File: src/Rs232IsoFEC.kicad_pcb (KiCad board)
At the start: 2 copper layers, 24 x 27.9 mm, 24 parts, among them J1 B3B-XH-A, P1 105444-0001, Q1 DMP3099L-13, U1 FT232RL, U2 ADM3251E

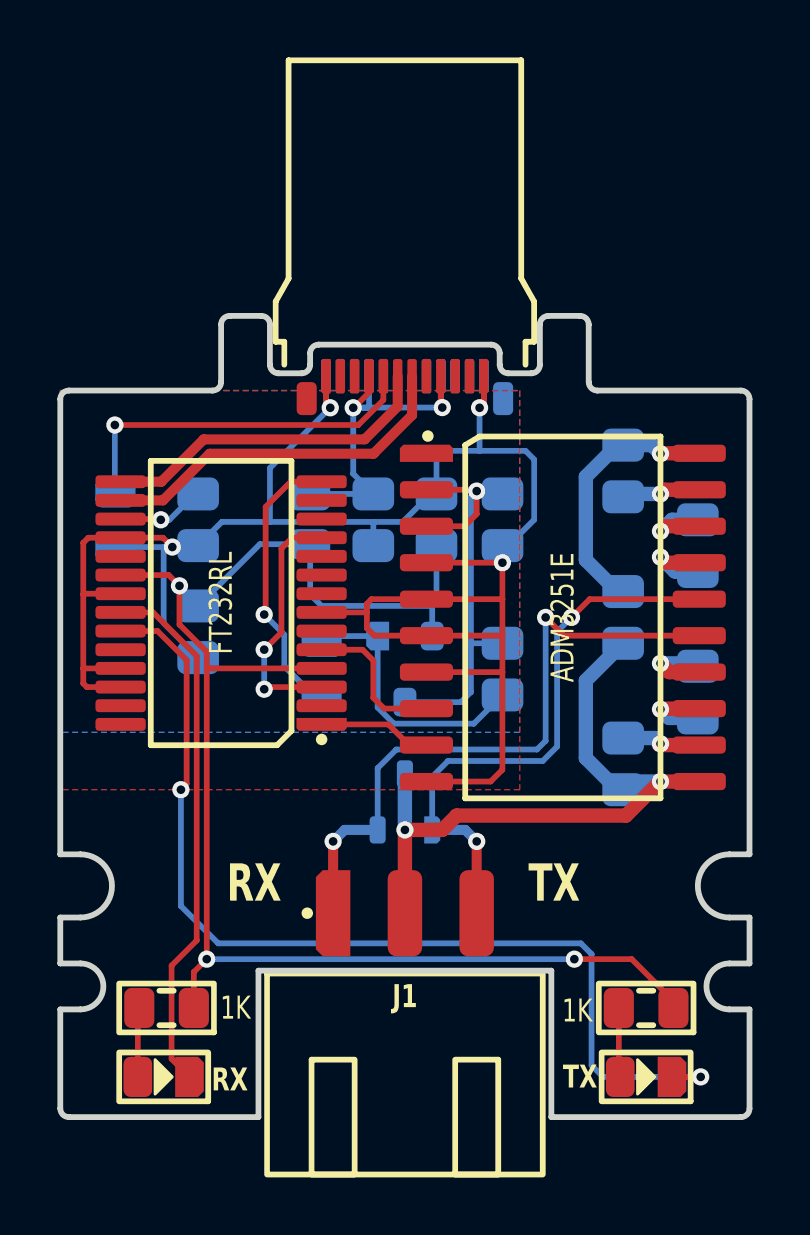
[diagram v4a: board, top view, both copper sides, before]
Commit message: Changed protection diode
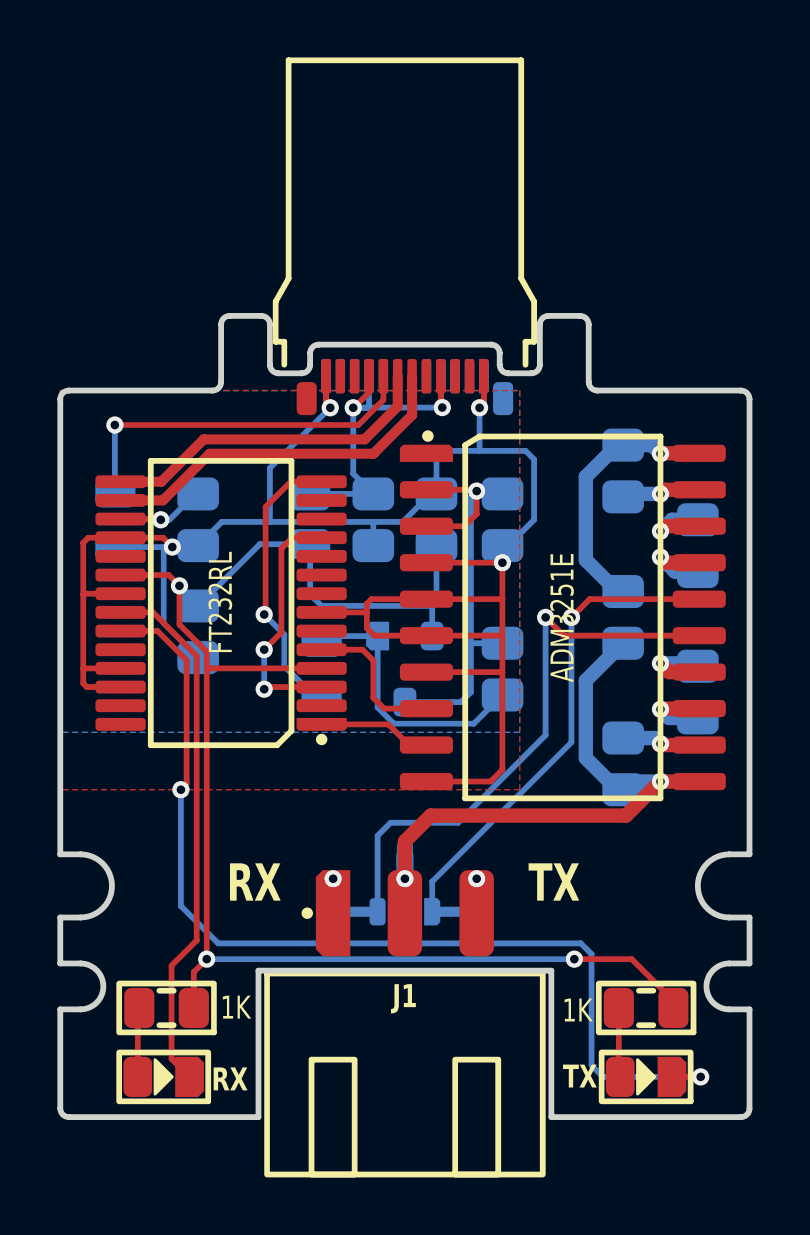
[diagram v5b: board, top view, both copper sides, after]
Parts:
- D1: value SM12T1G -> PESD12VL2BT
- moved D1 2.85 mm to (32.0, 39.8)
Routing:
- net ISO_GND: track 22.9 -> 20.3 mm
- net ISO_TXD: track 20.3 -> 19.7 mm
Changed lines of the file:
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@@
   )
   (footprint "Medo64:D TVS SM05T1G (SOT23-3)" (layer "B.Cu")
-    (at 32 36.925 180)
+    (at 32 39.775 180)
     (descr "SM05T1G [SM05T1GOSCT-ND]")
     (attr smd)
@@
         (effects (font (size 0.8 0.6) (thickness 0.15)) (justify mirror))
     )
-    (fp_text value "SM12T1G" (at 0 -2.2) (layer "B.SilkS") hide
+    (fp_text value "PESD12VL2BT" (at 0 -2.2) (layer "B.SilkS") hide
         (effects (font (size 0.8 0.6) (thickness 0.15)) (justify mirror))
     )
@@
   (segment (start 23.875 42.625) (end 23.875 45.875) (width 0.2) (layer "F.Cu") (net 13))
   (segment (start 22.1 30.325) (end 23.230026 30.325) (width 0.2) (layer "F.Cu") (net 13))
+  (segment (start 32.9 37.4) (end 39.7 37.4) (width 0.5) (layer "F.Cu") (net 14))
+  (segment (start 40.9 36.215) (end 42.25 36.215) (width 0.5) (layer "F.Cu") (net 14))
   (segment (start 40.885 36.215) (end 40.9 36.215) (width 0.5) (layer "F.Cu") (net 14))
-  (segment (start 33.8 37.4) (end 39.7 37.4) (width 0.5) (layer "F.Cu") (net 14))
-  (segment (start 32 37.9) (end 33.3 37.9) (width 0.5) (layer "F.Cu") (net 14))
-  (segment (start 33.3 37.9) (end 33.8 37.4) (width 0.5) (layer "F.Cu") (net 14))
+  (segment (start 32 38.3) (end 32.9 37.4) (width 0.5) (layer "F.Cu") (net 14))
   (segment (start 39.7 37.4) (end 40.885 36.215) (width 0.5) (layer "F.Cu") (net 14))
-  (segment (start 40.9 36.215) (end 42.25 36.215) (width 0.5) (layer "F.Cu") (net 14))
-  (segment (start 32 40.8) (end 32 37.9) (width 0.5) (layer "F.Cu") (net 14))
-  (via (at 32 37.9) (size 0.6) (drill 0.3) (layers "F.Cu" "B.Cu") (net 14))
+  (segment (start 32 39.6) (end 32 38.3) (width 0.5) (layer "F.Cu") (net 14))
+  (via (at 32 39.6) (size 0.6) (drill 0.3) (layers "F.Cu" "B.Cu") (net 14))
   (via (at 40.9 36.215) (size 0.6) (drill 0.3) (layers "F.Cu" "B.Cu") (net 14))
   (segment (start 39.4 36.5) (end 38.3 35.4) (width 0.5) (layer "B.Cu") (net 14))
-  (segment (start 32 37.9) (end 32 35.95) (width 0.5) (layer "B.Cu") (net 14))
+  (segment (start 32 38.8) (end 32 39.6) (width 0.6) (layer "B.Cu") (net 14))
   (segment (start 38.3 35.4) (end 38.3 32.7) (width 0.5) (layer "B.Cu") (net 14))
   (segment (start 40.9 36.215) (end 39.885 36.215) (width 0.5) (layer "B.Cu") (net 14))
   (segment (start 38.3 32.7) (end 39.6 31.4) (width 0.5) (layer "B.Cu") (net 14))
-  (segment (start 29.5 40.8) (end 29.5 38.3) (width 0.35) (layer "F.Cu") (net 15))
   (segment (start 42.25 31.135) (end 37.535 31.135) (width 0.2) (layer "F.Cu") (net 15))
   (segment (start 37.535 31.135) (end 36.9 30.5) (width 0.2) (layer "F.Cu") (net 15))
-  (via (at 29.5 38.3) (size 0.6) (drill 0.3) (layers "F.Cu" "B.Cu") (net 15))
+  (via (at 29.5 39.6) (size 0.6) (drill 0.3) (layers "F.Cu" "B.Cu") (net 15))
   (via (at 36.9 30.5) (size 0.6) (drill 0.3) (layers "F.Cu" "B.Cu") (net 15))
-  (segment (start 29.9 37.9) (end 31.05 37.9) (width 0.35) (layer "B.Cu") (net 15))
-  (segment (start 36.9 34.8) (end 36.9 30.5) (width 0.2) (layer "B.Cu") (net 15))
-  (segment (start 31.05 35.75) (end 31.7 35.1) (width 0.2) (layer "B.Cu") (net 15))
-  (segment (start 31.7 35.1) (end 36.6 35.1) (width 0.2) (layer "B.Cu") (net 15))
-  (segment (start 29.5 38.3) (end 29.9 37.9) (width 0.35) (layer "B.Cu") (net 15))
-  (segment (start 36.6 35.1) (end 36.9 34.8) (width 0.2) (layer "B.Cu") (net 15))
-  (segment (start 31.05 37.9) (end 31.05 35.75) (width 0.2) (layer "B.Cu") (net 15))
+  (segment (start 31.05 38.1) (end 31.05 40.750002) (width 0.2) (layer "B.Cu") (net 15))
+  (segment (start 29.5 40.750002) (end 31.05 40.750002) (width 0.35) (layer "B.Cu") (net 15))
+  (segment (start 33.85 37.65) (end 31.5 37.65) (width 0.2) (layer "B.Cu") (net 15))
+  (segment (start 31.5 37.65) (end 31.05 38.1) (width 0.2) (layer "B.Cu") (net 15))
+  (segment (start 36.9 30.5) (end 36.9 34.6) (width 0.2) (layer "B.Cu") (net 15))
+  (segment (start 36.9 34.6) (end 33.85 37.65) (width 0.2) (layer "B.Cu") (net 15))
+  (segment (start 29.5 39.6) (end 29.5 40.750002) (width 0.35) (layer "B.Cu") (net 15))
   (segment (start 42.25 29.865) (end 38.435 29.865) (width 0.2) (layer "F.Cu") (net 16))
   (segment (start 38.435 29.865) (end 37.8 30.5) (width 0.2) (layer "F.Cu") (net 16))
-  (segment (start 34.5 40.8) (end 34.5 38.3) (width 0.35) (layer "F.Cu") (net 16))
-  (via (at 34.5 38.3) (size 0.6) (drill 0.3) (layers "F.Cu" "B.Cu") (net 16))
+  (via (at 34.5 39.6) (size 0.6) (drill 0.3) (layers "F.Cu" "B.Cu") (net 16))
   (via (at 37.8 30.5) (size 0.6) (drill 0.3) (layers "F.Cu" "B.Cu") (net 16))
-  (segment (start 32.95 37.9) (end 32.95 36.05) (width 0.2) (layer "B.Cu") (net 16))
-  (segment (start 33.5 35.5) (end 36.8 35.5) (width 0.2) (layer "B.Cu") (net 16))
-  (segment (start 37.3 35) (end 37.3 31) (width 0.2) (layer "B.Cu") (net 16))
-  (segment (start 34.1 37.9) (end 32.95 37.9) (width 0.35) (layer "B.Cu") (net 16))
-  (segment (start 37.3 31) (end 37.8 30.5) (width 0.2) (layer "B.Cu") (net 16))
-  (segment (start 34.5 38.3) (end 34.1 37.9) (width 0.35) (layer "B.Cu") (net 16))
-  (segment (start 32.95 36.05) (end 33.5 35.5) (width 0.2) (layer "B.Cu") (net 16))
-  (segment (start 36.8 35.5) (end 37.3 35) (width 0.2) (layer "B.Cu") (net 16))
+  (segment (start 34.5 39.6) (end 34.5 40.750002) (width 0.35) (layer "B.Cu") (net 16))
+  (segment (start 34.5 40.750002) (end 32.95 40.750002) (width 0.35) (layer "B.Cu") (net 16))
+  (segment (start 32.95 39.7) (end 32.95 40.750002) (width 0.2) (layer "B.Cu") (net 16))
+  (segment (start 37.8 34.85) (end 32.95 39.7) (width 0.2) (layer "B.Cu") (net 16))
+  (segment (start 37.8 30.5) (end 37.8 34.85) (width 0.2) (layer "B.Cu") (net 16))
   (segment (start 41.045 26.055) (end 40.9 26.2) (width 0.5) (layer "F.Cu") (net 17))
   (segment (start 42.25 26.055) (end 41.045 26.055) (width 0.5) (layer "F.Cu") (net 17))

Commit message: Minor refactoring
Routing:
- net ISO_TXD: track 19.7 -> 18.5 mm
- net ISO_RXD: track 22.4 -> 21.2 mm
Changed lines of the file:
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@@
     (descr "SM05T1G [SM05T1GOSCT-ND]")
     (attr smd)
-    (fp_text reference "D1" (at -1.2 1.425) (layer "B.SilkS")
+    (fp_text reference "D1" (at 0 -0.975) (layer "B.SilkS")
         (effects (font (size 0.8 0.6) (thickness 0.15)) (justify mirror))
     )
@@
   (gr_circle locked (center 20.7 39.85) (end 23.15 39.85)
     (stroke (width 0.01) (type solid)) (fill none) (layer "Margin"))
-  (gr_text "Rs232IsoFEC A" (at 32 41.8) (layer "B.SilkS")
+  (gr_text "Rs232IsoFEC A" (at 32 37.5) (layer "B.SilkS")
     (effects (font (size 0.8 0.6) (thickness 0.15) bold) (justify mirror))
   )
-  (gr_text "RX" (at 27.7 39) (layer "F.SilkS" knockout)
+  (gr_text "RX" (at 27.95 39) (layer "F.SilkS" knockout)
     (effects (font (size 1.3 0.9) (thickness 0.15) bold) (justify right top))
   )
-  (gr_text "TX" (at 36.3 39) (layer "F.SilkS" knockout)
+  (gr_text "TX" (at 36.05 39) (layer "F.SilkS" knockout)
     (effects (font (size 1.3 0.9) (thickness 0.15) bold) (justify left top))
   )
@@
   (segment (start 42.25 31.135) (end 37.535 31.135) (width 0.2) (layer "F.Cu") (net 15))
   (segment (start 37.535 31.135) (end 36.9 30.5) (width 0.2) (layer "F.Cu") (net 15))
-  (via (at 29.5 39.6) (size 0.6) (drill 0.3) (layers "F.Cu" "B.Cu") (net 15))
+  (via (at 29.5 40.75) (size 0.6) (drill 0.3) (layers "F.Cu" "B.Cu") (net 15))
   (via (at 36.9 30.5) (size 0.6) (drill 0.3) (layers "F.Cu" "B.Cu") (net 15))
   (segment (start 31.05 38.1) (end 31.05 40.750002) (width 0.2) (layer "B.Cu") (net 15))
-  (segment (start 29.5 40.750002) (end 31.05 40.750002) (width 0.35) (layer "B.Cu") (net 15))
+  (segment (start 29.5 40.75) (end 29.500002 40.750002) (width 0.35) (layer "B.Cu") (net 15))
   (segment (start 33.85 37.65) (end 31.5 37.65) (width 0.2) (layer "B.Cu") (net 15))
   (segment (start 31.5 37.65) (end 31.05 38.1) (width 0.2) (layer "B.Cu") (net 15))
+  (segment (start 29.500002 40.750002) (end 31.05 40.750002) (width 0.35) (layer "B.Cu") (net 15))
   (segment (start 36.9 30.5) (end 36.9 34.6) (width 0.2) (layer "B.Cu") (net 15))
   (segment (start 36.9 34.6) (end 33.85 37.65) (width 0.2) (layer "B.Cu") (net 15))
-  (segment (start 29.5 39.6) (end 29.5 40.750002) (width 0.35) (layer "B.Cu") (net 15))
   (segment (start 42.25 29.865) (end 38.435 29.865) (width 0.2) (layer "F.Cu") (net 16))
   (segment (start 38.435 29.865) (end 37.8 30.5) (width 0.2) (layer "F.Cu") (net 16))
-  (via (at 34.5 39.6) (size 0.6) (drill 0.3) (layers "F.Cu" "B.Cu") (net 16))
+  (via (at 34.5 40.75) (size 0.6) (drill 0.3) (layers "F.Cu" "B.Cu") (net 16))
   (via (at 37.8 30.5) (size 0.6) (drill 0.3) (layers "F.Cu" "B.Cu") (net 16))
-  (segment (start 34.5 39.6) (end 34.5 40.750002) (width 0.35) (layer "B.Cu") (net 16))
-  (segment (start 34.5 40.750002) (end 32.95 40.750002) (width 0.35) (layer "B.Cu") (net 16))
   (segment (start 32.95 39.7) (end 32.95 40.750002) (width 0.2) (layer "B.Cu") (net 16))
   (segment (start 37.8 34.85) (end 32.95 39.7) (width 0.2) (layer "B.Cu") (net 16))
   (segment (start 37.8 30.5) (end 37.8 34.85) (width 0.2) (layer "B.Cu") (net 16))
+  (segment (start 34.5 40.75) (end 34.499998 40.750002) (width 0.35) (layer "B.Cu") (net 16))
+  (segment (start 34.499998 40.750002) (end 32.95 40.750002) (width 0.35) (layer "B.Cu") (net 16))
   (segment (start 41.045 26.055) (end 40.9 26.2) (width 0.5) (layer "F.Cu") (net 17))
   (segment (start 42.25 26.055) (end 41.045 26.055) (width 0.5) (layer "F.Cu") (net 17))

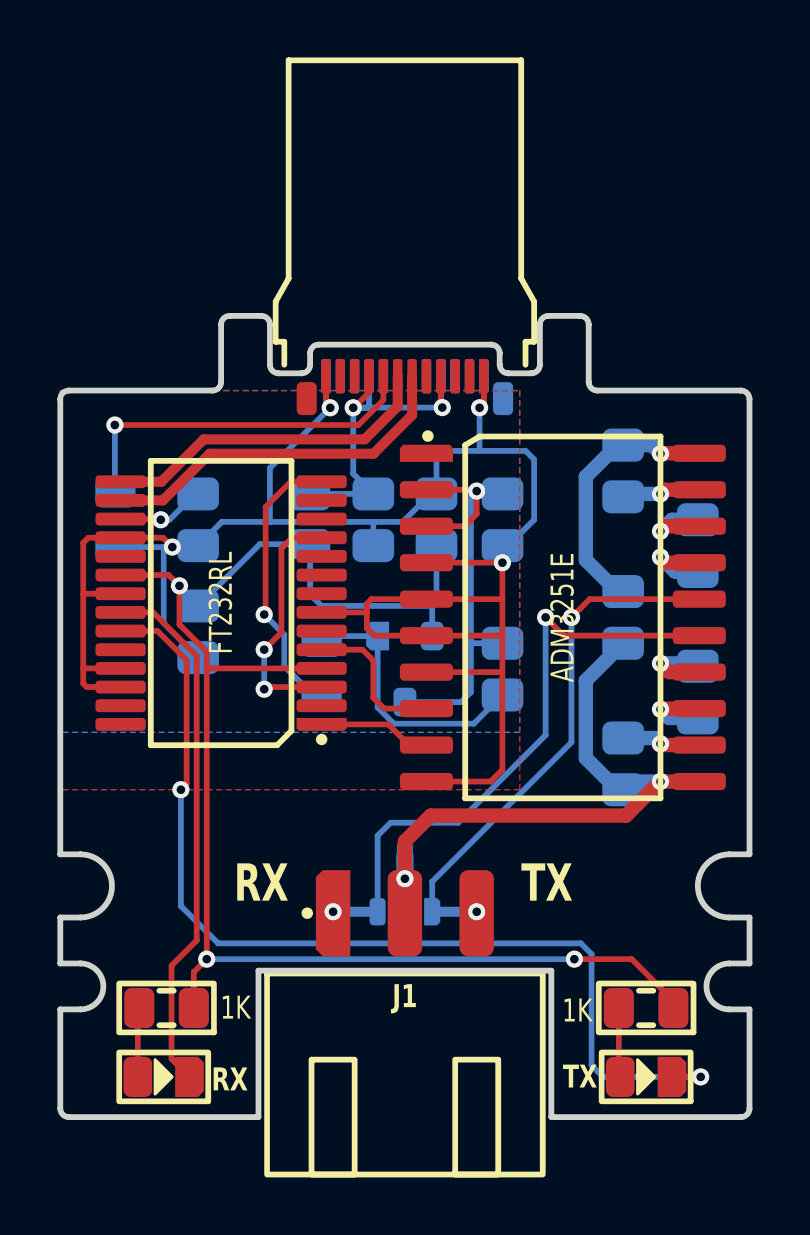
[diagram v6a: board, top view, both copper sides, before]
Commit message: Moved LEDs to bottom
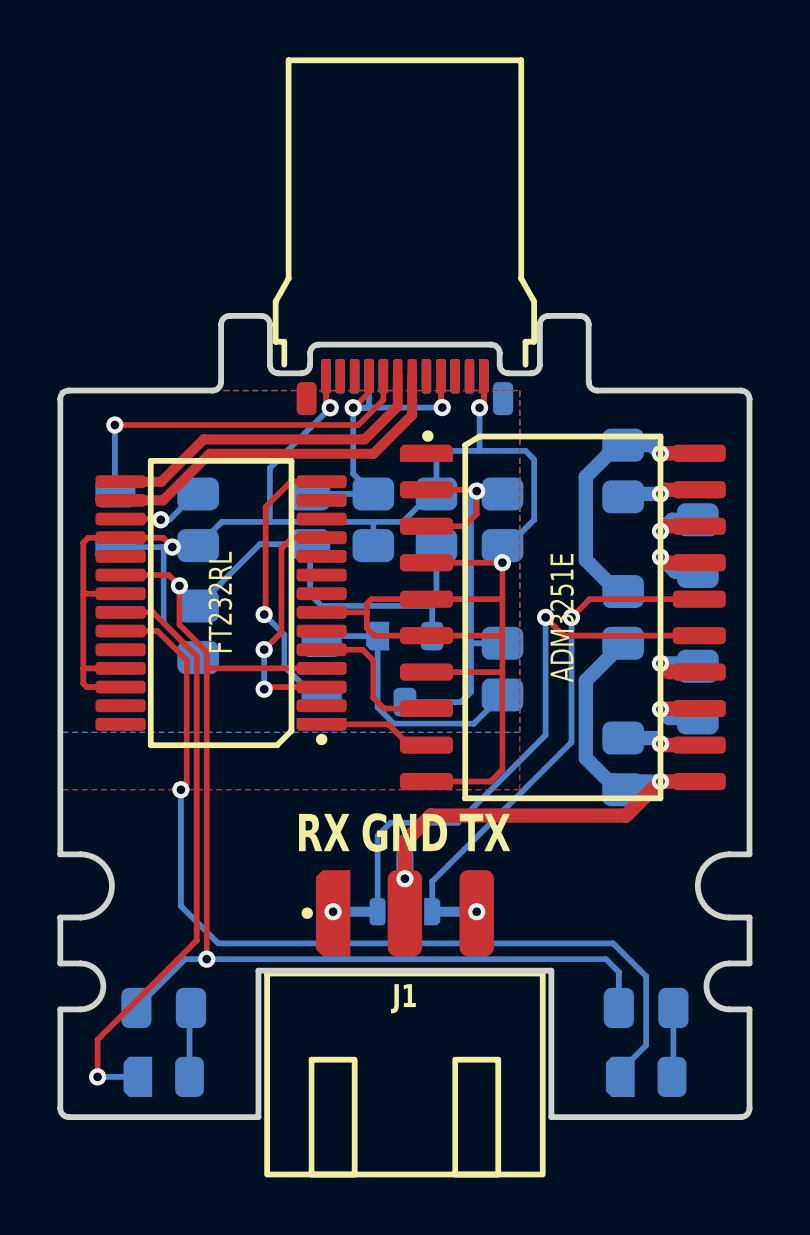
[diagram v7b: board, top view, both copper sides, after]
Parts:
- DS1, DS2, R1, R2: moved to B.Cu
- moved R1 0.10 mm to (23.6, 44.1), turned to 0 degrees
- turned DS1 to 0 degrees
- turned DS2 to 0 degrees
- turned R2 to 0 degrees
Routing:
- net LED_TXD: track 35.2 -> 32.3 mm, vias 2 -> 1
- net LED_RXD: track 18.6 -> 20.8 mm, vias 0 -> 1
- net 5V: track 53.9 -> 54.1 mm, vias 3 -> 2
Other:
- board text added: "GND"

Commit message: Added PWREN pullup and moved LED 5V to switched
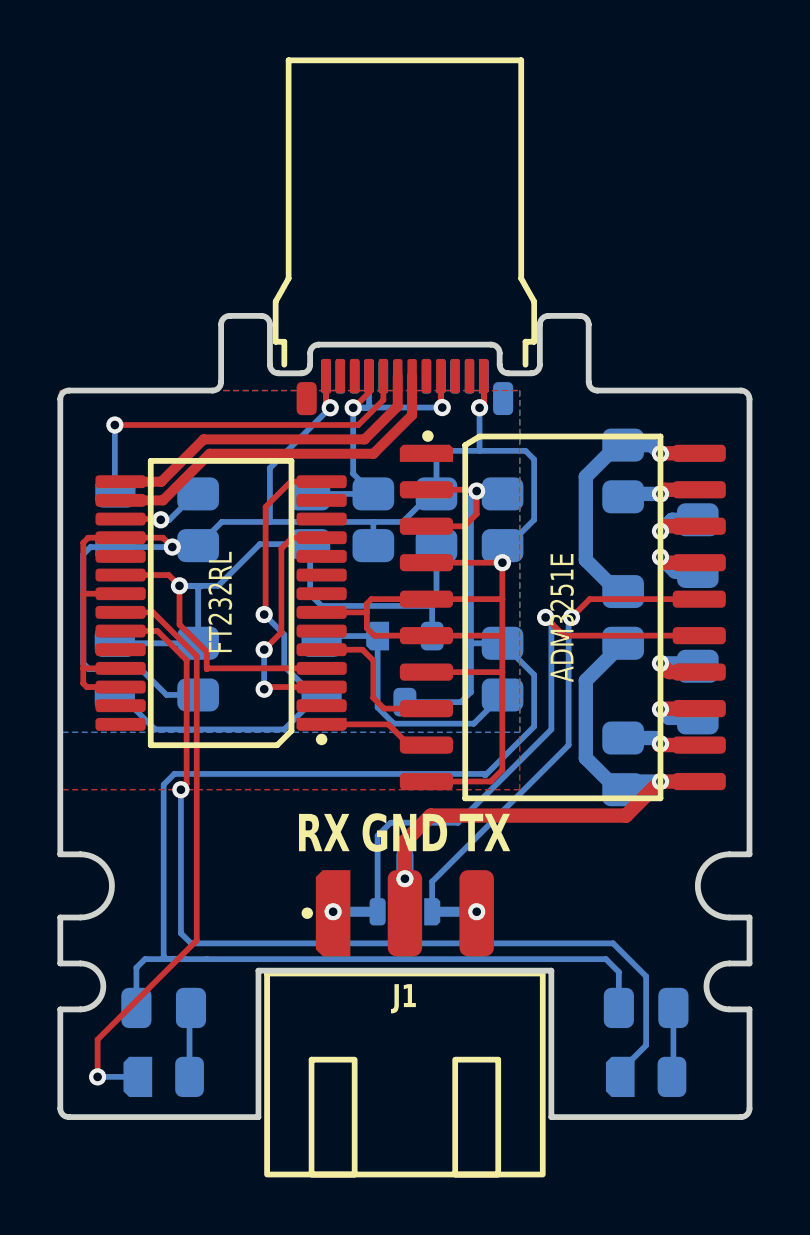
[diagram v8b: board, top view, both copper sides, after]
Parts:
- added R5: 10K, Medo64:R (0805), B.Cu at (21.9, 32.3)
- moved C2 1.30 mm to (24.8, 32.3)
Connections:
- R1 pad 1: 5V -> 5V_SW
- R2 pad 1: 5V -> 5V_SW
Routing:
- net 5V_SW: track 15.9 -> 59.6 mm
- net 5V: track 54.1 -> 29.9 mm, vias 2 -> 1
- net PWREN#: track 9.66 -> 17.4 mm
- net GND: track 78.3 -> 83.4 mm
- net LED_TXD: track 32.3 -> 32.8 mm
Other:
- board text added: "Rs232IsoFEC B"
- board text removed: "Rs232IsoFEC A"
